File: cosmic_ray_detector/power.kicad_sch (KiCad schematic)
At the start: 16 parts

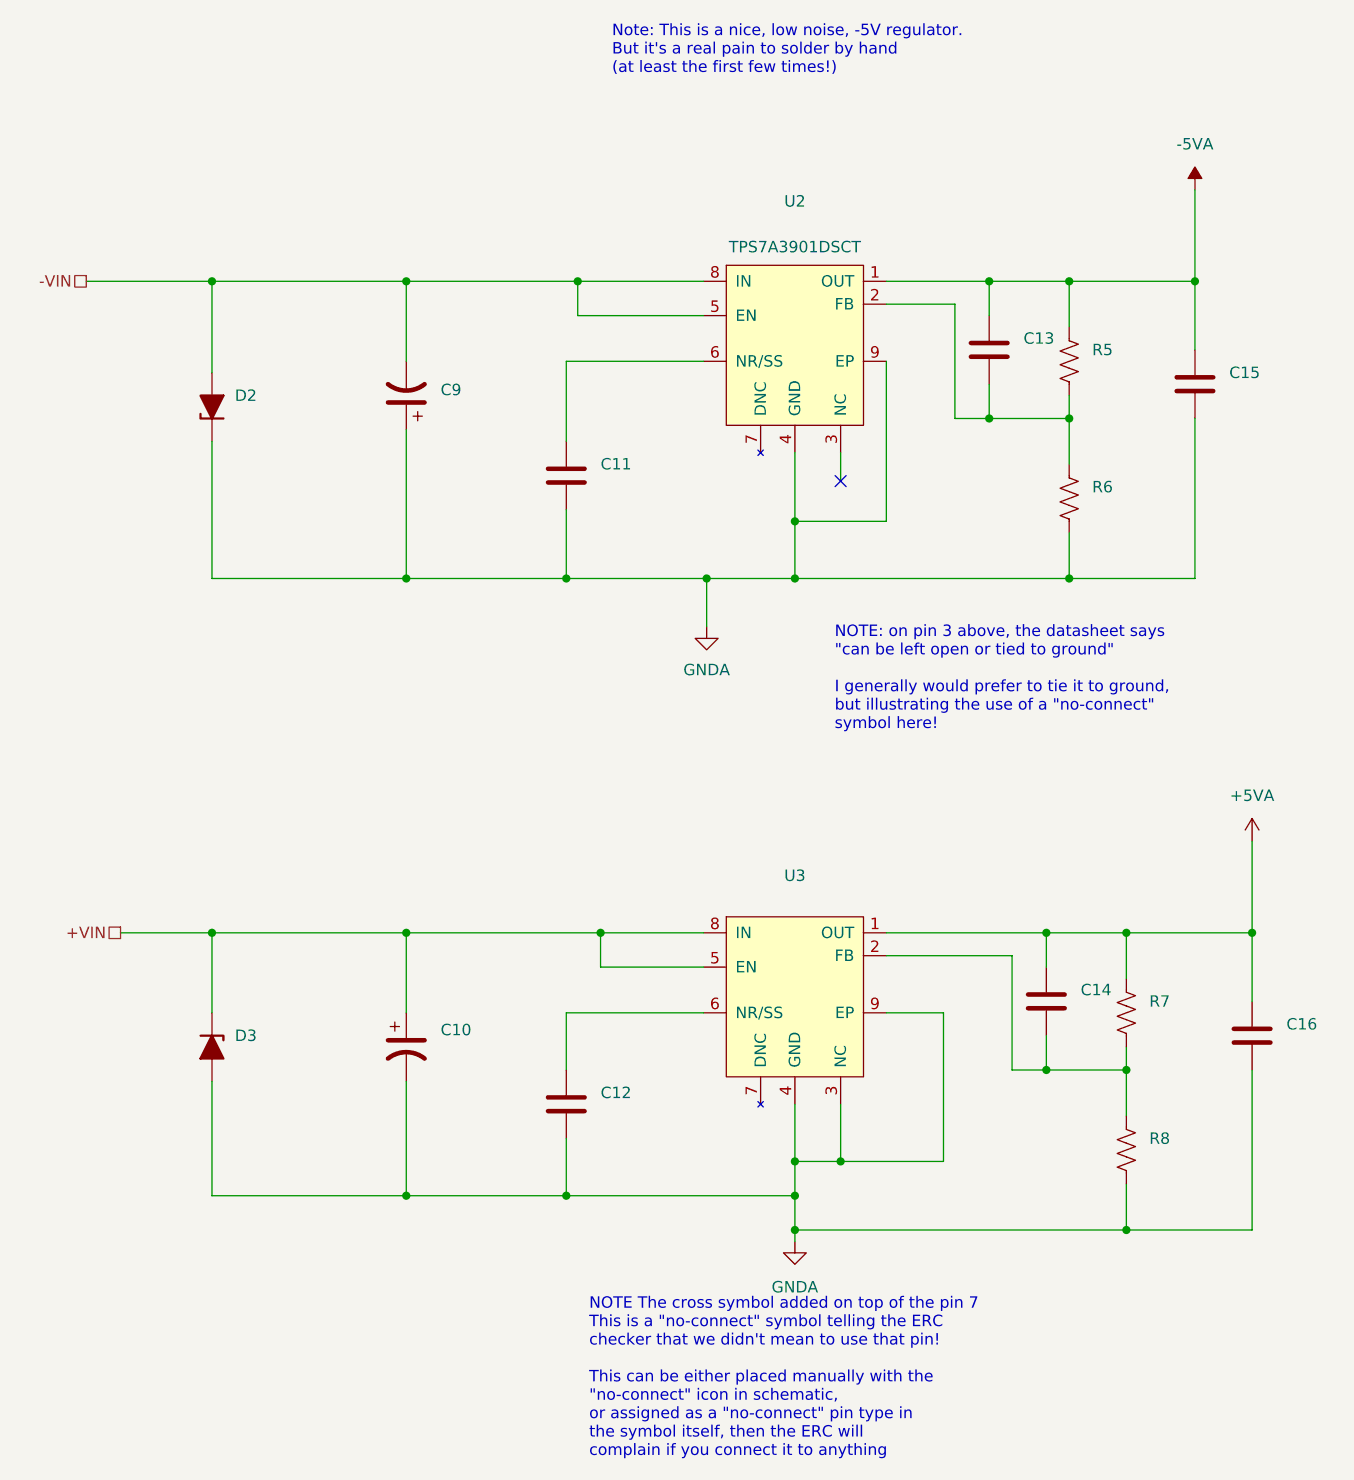
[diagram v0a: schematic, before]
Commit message: update routed / finished PCB to version 9
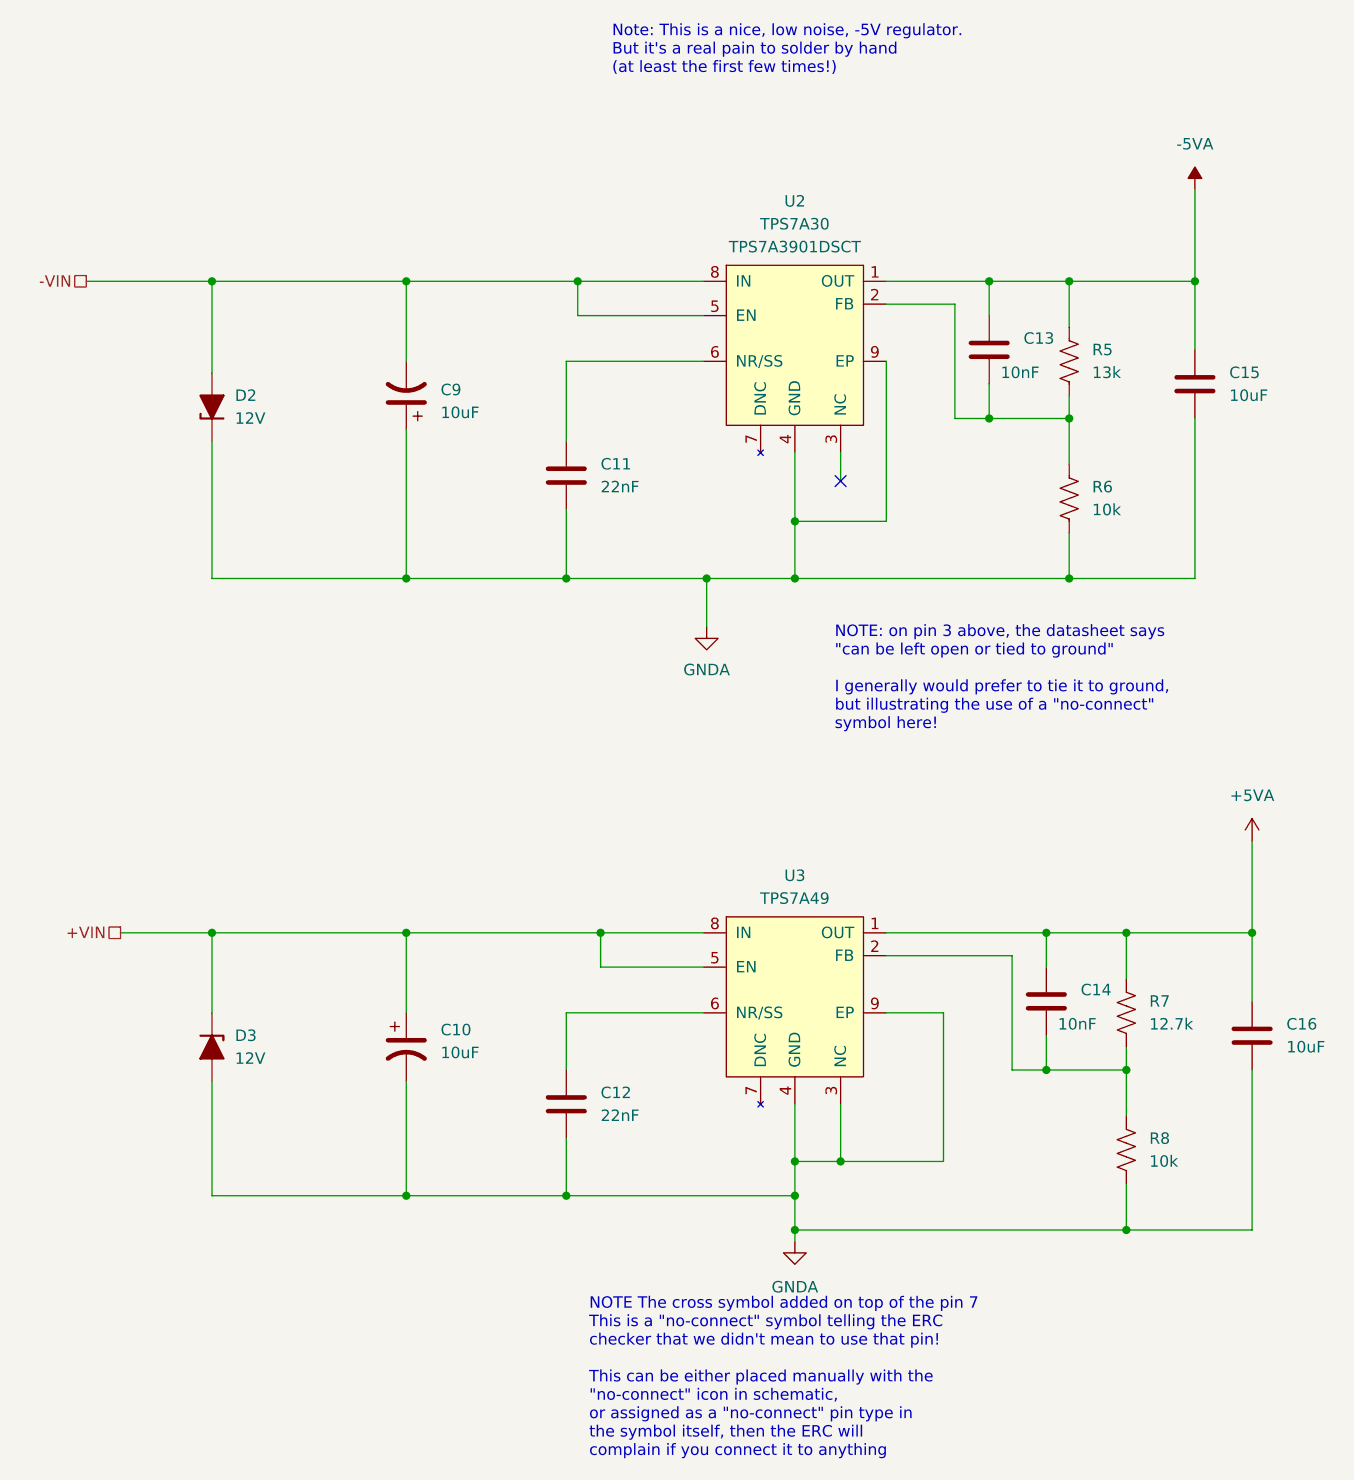
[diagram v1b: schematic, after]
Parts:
- C10, C15, C16, C9: value (none) -> 10uF; footprint (none) -> cosmic_ray_detector_lib:MAL215375109E3
- C11, C12: value (none) -> 22nF; footprint (none) -> Capacitor_SMD:C_0402_1005Metric
- C13, C14: value (none) -> 10nF; footprint (none) -> Capacitor_SMD:C_0402_1005Metric
- D2, D3: value (none) -> 12V; footprint (none) -> Diode_SMD:D_SOD-123
- R5: value (none) -> 13k; footprint (none) -> Resistor_SMD:R_0402_1005Metric
- R6, R8: value (none) -> 10k; footprint (none) -> Resistor_SMD:R_0402_1005Metric
- R7: value (none) -> 12.7k; footprint (none) -> Resistor_SMD:R_0402_1005Metric
- U2: value (none) -> TPS7A30; footprint (none) -> cosmic_ray_detector_lib:MSOP-8-1EP_3x3mm_P0.65mm_EP1.73x1.85mm_ThermalVias
- U3: value (none) -> TPS7A49; footprint (none) -> cosmic_ray_detector_lib:MSOP-8-1EP_3x3mm_P0.65mm_EP1.73x1.85mm_ThermalVias

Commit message: update pcb and schem to V10
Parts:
- C11, C12, C13, C14: footprint Capacitor_SMD:C_0402_1005Metric -> cosmic_ray_detector_lib:C_0402_1005Metric
- C16: Farnell (none) -> 1187014; MPN (none) -> MAL215375109E3; Manufacturer_Name (none) -> Vishay
- D2, D3: footprint Diode_SMD:D_SOD-123 -> cosmic_ray_detector_lib:D_SOD-123
- R5, R6, R7, R8: footprint Resistor_SMD:R_0402_1005Metric -> cosmic_ray_detector_lib:R_0402_1005Metric
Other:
- title: (none) -> AITL Simple Cosmic Ray Detector
